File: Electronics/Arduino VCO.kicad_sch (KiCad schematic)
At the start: 39 parts, among them U1 TL072

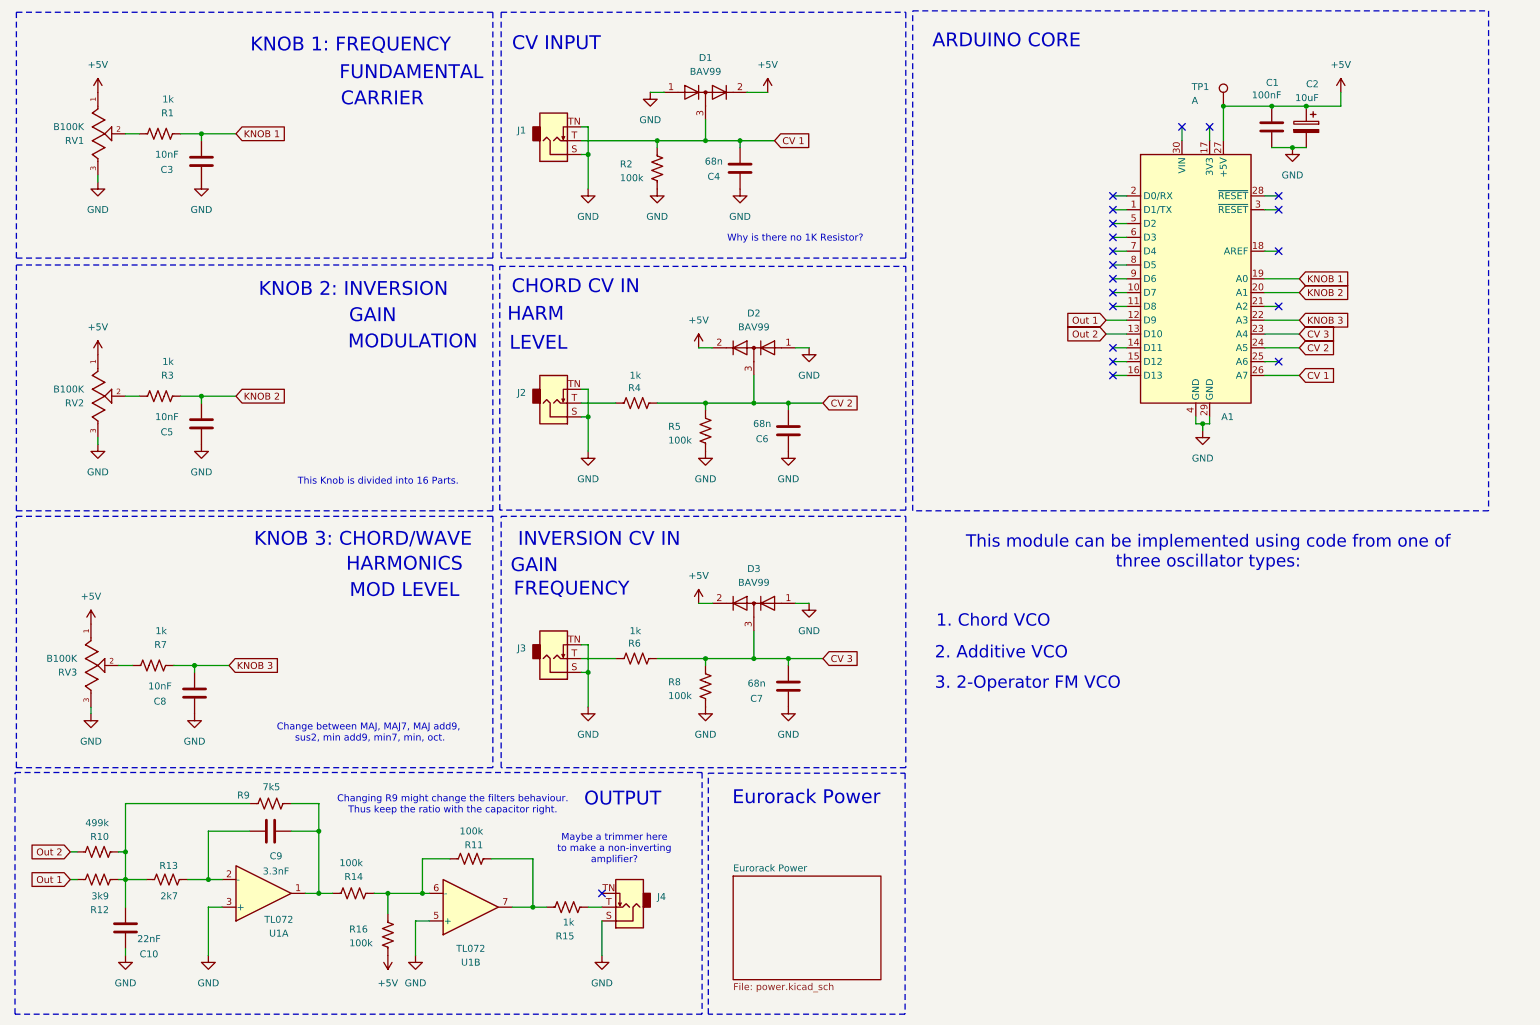
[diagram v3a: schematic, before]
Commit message: adding further testpoints
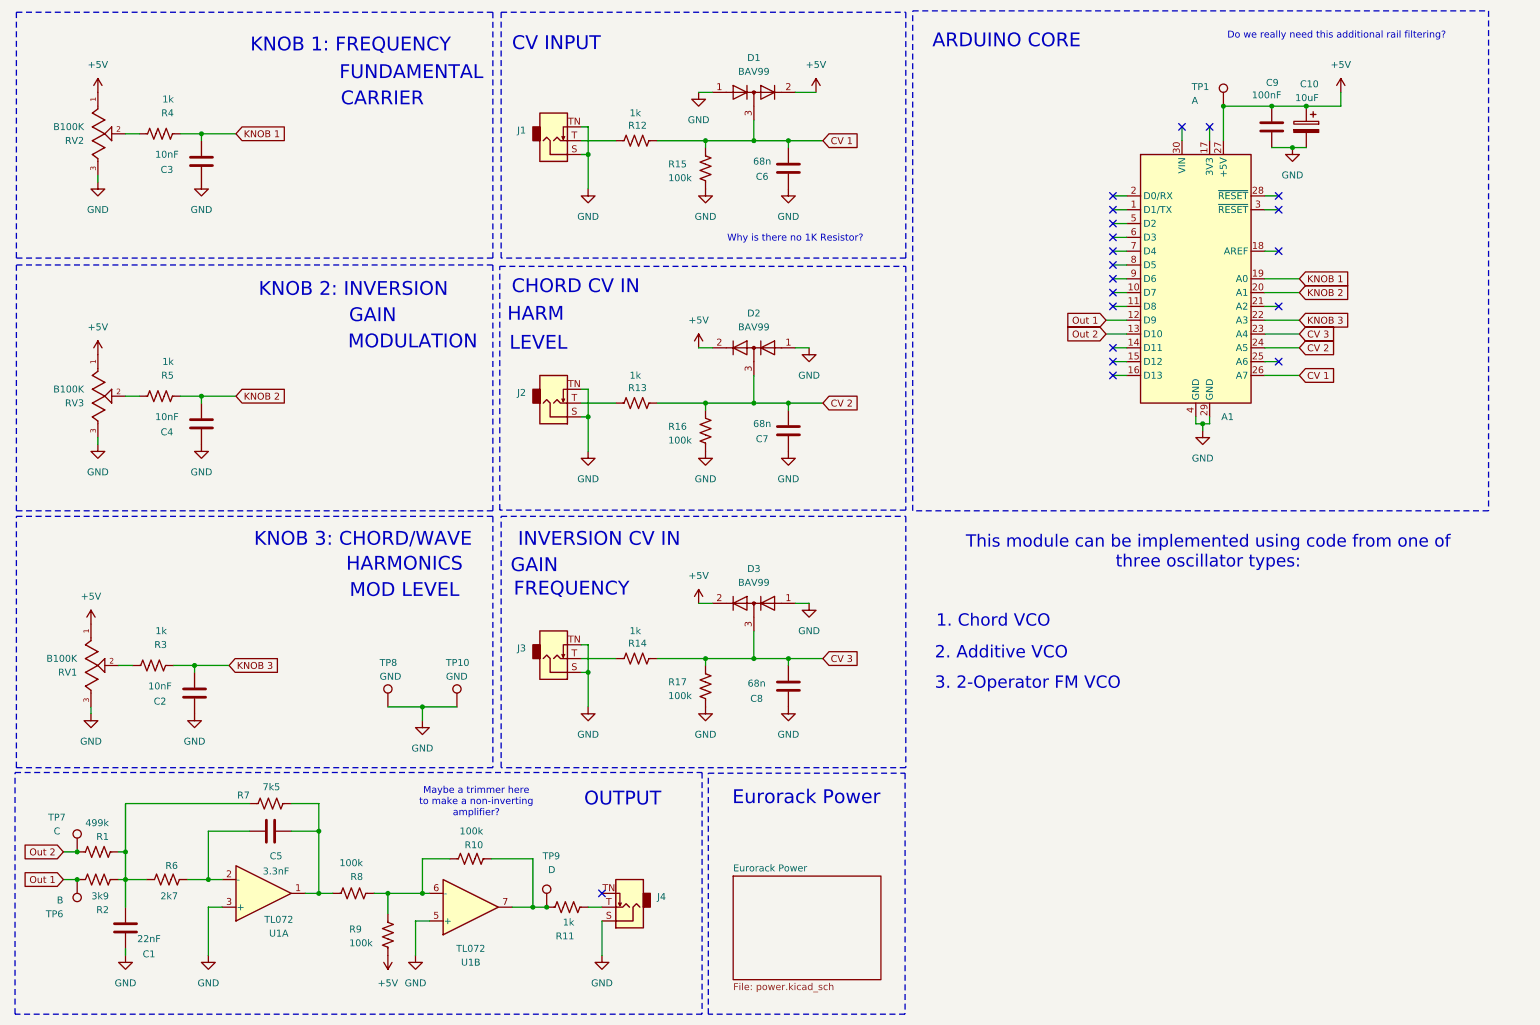
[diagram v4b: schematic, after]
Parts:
- added R12: 1k, Resistor_SMD:R_0805_2012Metric_Pad1.20x1.40mm_HandSolder, symbol Device:R_US
- added TP10, TP8: GND, TestPoint:TestPoint_Pad_D1.5mm, symbol Connector:TestPoint
- added TP6: B, TestPoint:TestPoint_Pad_D1.5mm, symbol Connector:TestPoint
- added TP7: C, TestPoint:TestPoint_Pad_D1.5mm, symbol Connector:TestPoint
- added TP9: D, TestPoint:TestPoint_Pad_D1.5mm, symbol Connector:TestPoint
- renumbered C10 to C1, C2 to C10, C8 to C2, C5 to C4, C9 to C5, C4 to C6, C6 to C7, C7 to C8, C1 to C9, R10 to R1, R11 to R10, R15 to R11, R4 to R13, R6 to R14, R2 to R15, R5 to R16, R8 to R17, R12 to R2, R7 to R3, R1 to R4, R3 to R5, R13 to R6, R9 to R7, R14 to R8, R16 to R9, RV3 to RV1, RV1 to RV2, RV2 to RV3
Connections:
- net CV 1: now also R12.2; no longer J1.T
- net GND: now also TP10.1, TP8.1
- net Out 1: now also TP6.1
- net Out 2: now also TP7.1
- net at R10.2, R11.1, U1.7: now also TP9.1
- new net: J1.T, R12.1
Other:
- note added: "Do we really need this additional rail filtering?"
- note removed: "Change between MAJ, MAJ7, MAJ add9, sus2, min add9, min7, min, oct."
- note removed: "Changing R9 might change the filters behaviour. Thus keep the ratio with the capacitor right."
- note removed: "This Knob is divided into 16 Parts."
- moved on the sheet: C6, D1, R15

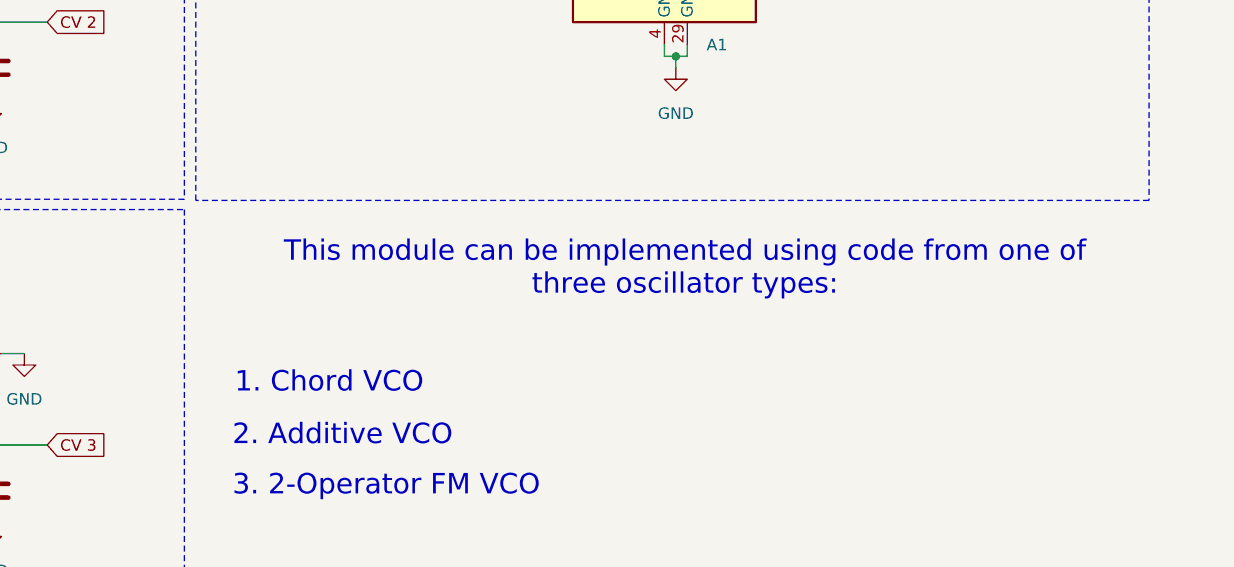
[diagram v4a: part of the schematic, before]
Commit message: leaving a remark of the firmwares on the schematics
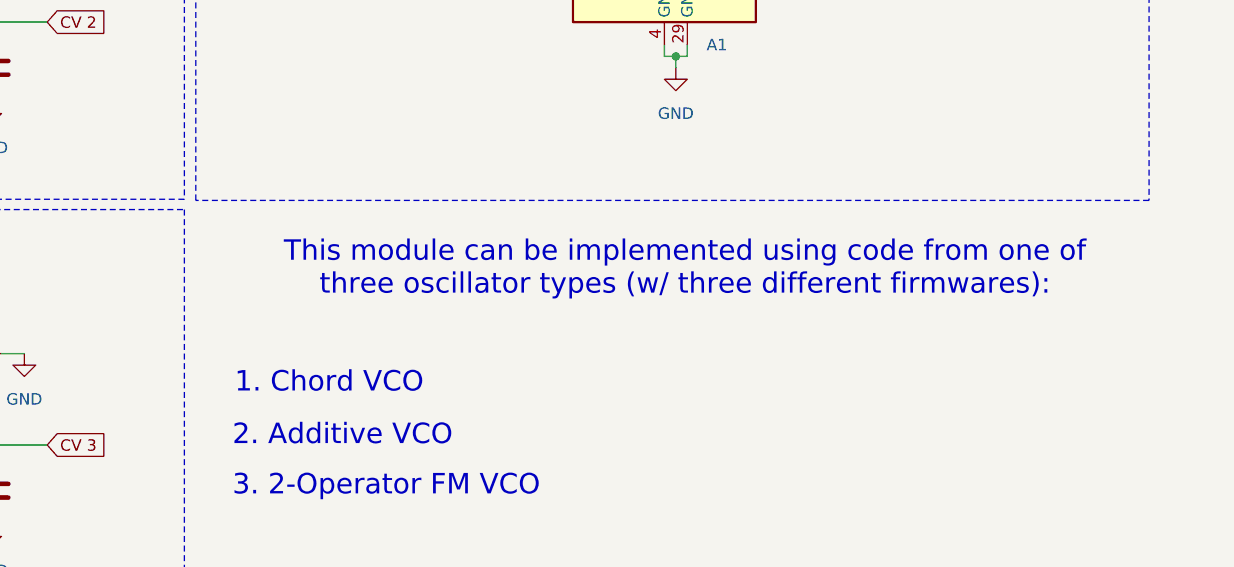
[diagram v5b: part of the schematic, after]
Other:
- note added: "This module can be implemented using code from one of three oscillator types (w/ three different firmwares):"
- note removed: "This module can be implemented using code from one of three oscillator types:"

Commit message: deleting unused files
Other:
- note removed: "Maybe a trimmer here to make a non-inverting amplifier?"
- note removed: "Why is there no 1K Resistor?"
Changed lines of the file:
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@@
-		)
-	)
-	(text "Why is there no 1K Resistor? "
-		(exclude_from_sim no)
-		(at 156.21 54.864 0)
-		(effects
-			(font
-				(size 1.27 1.27)
-				(color 255 0 0 1)
-			)
 		)
 	)
@@
 			)
 		)
-	)
-	(text "Maybe a trimmer here\nto make a non-inverting \namplifier?"
-		(exclude_from_sim no)
-		(at 97.536 158.496 0)
-		(effects
-			(font
-				(size 1.27 1.27)
-				(color 255 0 0 1)
-			)
-		)
